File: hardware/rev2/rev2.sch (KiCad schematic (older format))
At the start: 39 parts, among them J1 Conn_01x09_Female, J2 RFM9X_header, J3 Conn_02x03_Odd_Even, U2 MPL3115A2, U3 Teensy3.6, U5 ADXL345BCCZ, U7 TPS2113ADRBR

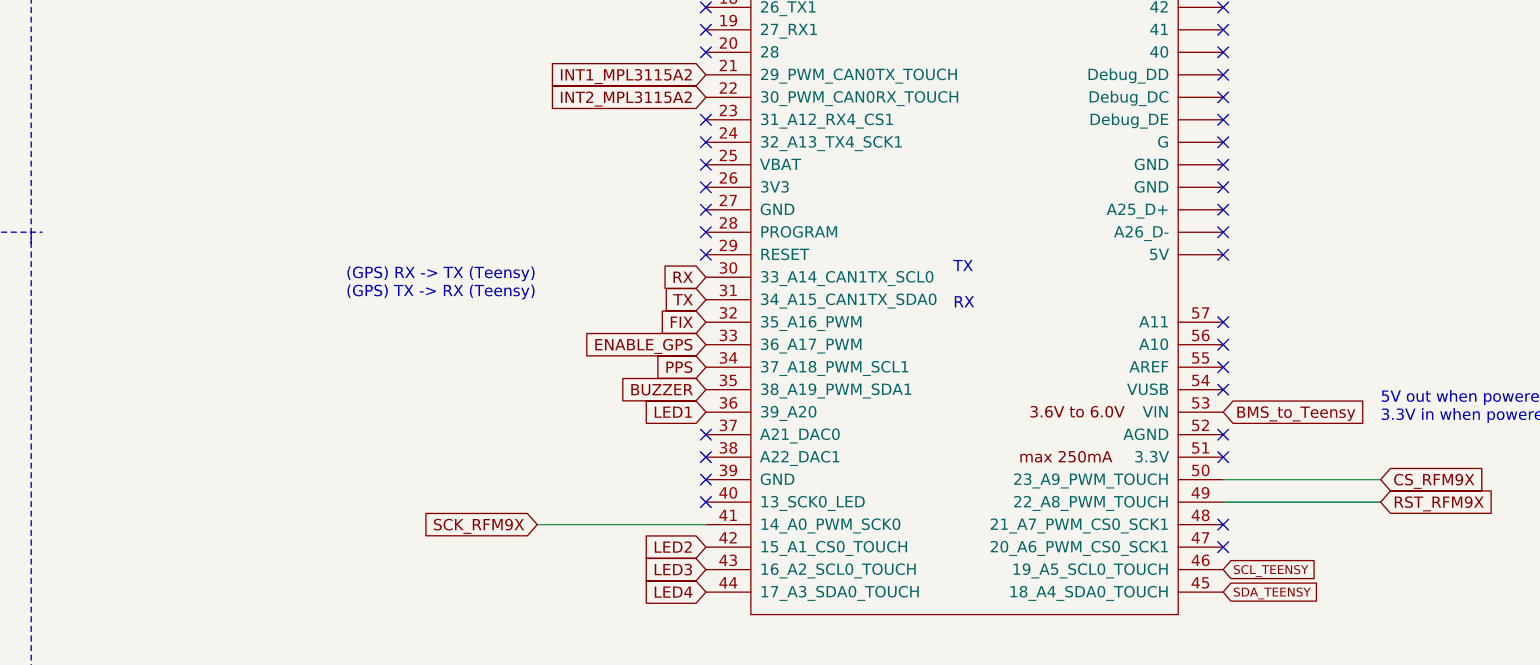
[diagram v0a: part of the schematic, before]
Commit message: connect LEDs to Teensy, add ground connections
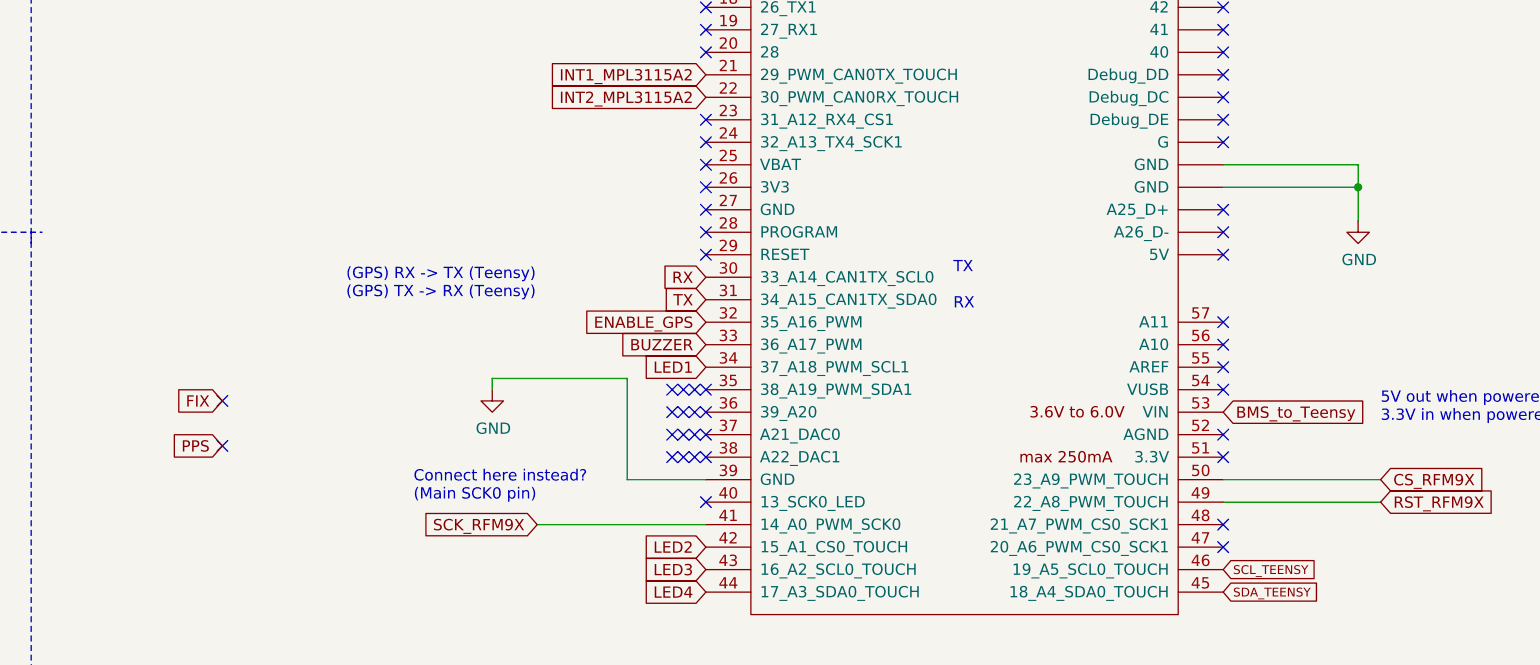
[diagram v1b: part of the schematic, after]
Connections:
- net BUZZER: now also U3.33 (36_A17_PWM); no longer U3.35 (38_A19_PWM_SDA1)
- net ENABLE_GPS: now also U3.32 (35_A16_PWM); no longer U3.33 (36_A17_PWM)
- net FIX: no longer U3.32 (35_A16_PWM)
- net GND: now also U3.39 (GND), U3.~ (GND)
- net LED1: now also U3.34 (37_A18_PWM_SCL1); no longer U3.36 (39_A20)
- net PPS: no longer U3.34 (37_A18_PWM_SCL1)
- no-connect marks 70 -> 83
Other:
- note added: "Connect here instead?\n(Main SCK0 pin)"
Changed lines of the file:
@@
 NoConn ~ 27650 10100
 NoConn ~ 27650 10200
-NoConn ~ 27650 10300
 NoConn ~ 27650 10400
 NoConn ~ 29950 10600
@@
 NoConn ~ 29950 9200
 NoConn ~ 29950 9100
-NoConn ~ 29950 9000
-NoConn ~ 29950 8900
 NoConn ~ 29950 8800
 NoConn ~ 29950 8700
@@
 TX
 Text GLabel 27650 9600 0    50   Input ~ 0
-FIX
-Text GLabel 27650 9700 0    50   Input ~ 0
 ENABLE_GPS
 NoConn ~ 29950 7100
@@
 NoConn ~ 29950 7400
 NoConn ~ 29950 7500
-Text GLabel 27650 9800 0    50   Input ~ 0
-PPS
 $Comp
 L Connector:Conn_01x09_Female J1
@@
 Wire Wire Line
 	25650 18900 25650 19050
-Text GLabel 27650 9900 0    50   Input ~ 0
+Text GLabel 27650 9700 0    50   Input ~ 0
 BUZZER
 NoConn ~ 27650 7300
@@
 Wire Wire Line
 	29550 15300 29550 15700
-Text GLabel 27650 10000 0    50   Input ~ 0
+Text GLabel 27650 9800 0    50   Input ~ 0
 LED1
 Text GLabel 27650 10600 0    50   Input ~ 0
@@
 Text GLabel 27650 10800 0    50   Input ~ 0
 LED4
+Text Notes 26350 10400 0    50   ~ 0
+Connect here instead?\n(Main SCK0 pin)
+Text GLabel 25500 10150 0    50   Input ~ 0
+PPS
+Text GLabel 25500 9950 0    50   Input ~ 0
+FIX
+NoConn ~ 27650 9900
+NoConn ~ 27650 10000
+NoConn ~ 25500 9950
+NoConn ~ 25500 10150
+NoConn ~ 27600 9900
+NoConn ~ 27550 9900
+NoConn ~ 27500 9900
+NoConn ~ 27600 10000
+NoConn ~ 27550 10000
+NoConn ~ 27500 10000
+NoConn ~ 27600 10100
+NoConn ~ 27550 10100
+NoConn ~ 27500 10100
+NoConn ~ 27600 10200
+NoConn ~ 27550 10200
+NoConn ~ 27500 10200
+$Comp
+L power:GND #PWR?
+U 1 1 606E440E
+P 26700 9900
+F 0 "#PWR?" H 26700 9650 50  0001 C CNN
+F 1 "GND" H 26705 9727 50  0000 C CNN
+F 2 "" H 26700 9900 50  0001 C CNN
+F 3 "" H 26700 9900 50  0001 C CNN
+	1    26700 9900
+	1    0    0    -1
+$EndComp
+Wire Wire Line
+	27650 10300 27300 10300
+Wire Wire Line
+	27300 10300 27300 9850
+Wire Wire Line
+	27300 9850 26700 9850
+Wire Wire Line
+	26700 9850 26700 9900
+Wire Wire Line
+	29950 8900 30550 8900
+Wire Wire Line
+	29950 9000 30550 9000
+$Comp
+L power:GND #PWR?
+U 1 1 606F48A4
+P 30550 9150
+F 0 "#PWR?" H 30550 8900 50  0001 C CNN
+F 1 "GND" H 30555 8977 50  0000 C CNN
+F 2 "" H 30550 9150 50  0001 C CNN
+F 3 "" H 30550 9150 50  0001 C CNN
+	1    30550 9150
+	1    0    0    -1
+$EndComp
+Wire Wire Line
+	30550 8900 30550 9000
+Wire Wire Line
+	30550 9000 30550 9150
+Connection ~ 30550 9000
 $EndSCHEMATC

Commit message: add KingpinLED footprint
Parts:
- D1: renamed from D?; symbol Device:D_Zener -> Device:D_Zener_x2_KCom_AAK
- D2, D3, D4, D5, D6, D7: renamed from D?; footprint (none) -> KingbrightLED:AA3528LSECKT-J4
- R10, R11, R12, R4, R8, R9: renamed from R?; footprint (none) -> footprints:R_0805_OEM
- gave numbers to parts that had none: 2
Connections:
- net BMS_to_Teensy: now also D1.3 (K); no longer D1.1 (K)
- net GND: now also D1.1 (A); no longer D1.2 (A)
- no-connect marks 83 -> 84
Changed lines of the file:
@@
 NoConn ~ 27650 6600
 $Comp
-L Device:LED D?
+L Device:LED D3
 U 1 1 6067C279
 P 24750 19750
-F 0 "D?" V 24789 19632 50  0000 R CNN
+F 0 "D3" V 24789 19632 50  0000 R CNN
 F 1 "LED" V 24698 19632 50  0000 R CNN
-F 2 "" H 24750 19750 50  0001 C CNN
+F 2 "KingbrightLED:AA3528LSECKT-J4" H 24750 19750 50  0001 C CNN
 F 3 "~" H 24750 19750 50  0001 C CNN
 	1    24750 19750
@@
 $EndComp
 $Comp
-L Device:LED D?
+L Device:LED D2
 U 1 1 60683FF2
 P 22700 19550
-F 0 "D?" V 22647 19630 50  0000 L CNN
+F 0 "D2" V 22647 19630 50  0000 L CNN
 F 1 "LED" V 22738 19630 50  0000 L CNN
-F 2 "" H 22700 19550 50  0001 C CNN
+F 2 "KingbrightLED:AA3528LSECKT-J4" H 22700 19550 50  0001 C CNN
 F 3 "~" H 22700 19550 50  0001 C CNN
 	1    22700 19550
@@
 $EndComp
 $Comp
-L Device:D_Zener D?
-U 1 1 60685331
-P 14000 19350
-F 0 "D?" V 13954 19430 50  0000 L CNN
-F 1 "D_Zener" V 14045 19430 50  0000 L CNN
-F 2 "Package_TO_SOT_SMD:SOT-23" H 14000 19350 50  0001 C CNN
-F 3 "http://www.smc-diodes.com/propdf/S23C03%20THRU%20S23C36%20N1001%20REV.A.pdf" H 14000 19350 50  0001 C CNN
-	1    14000 19350
-	0    1    1    0
-$EndComp
-$Comp
-L Device:R R?
+L Device:R R3
 U 1 1 60685DD7
 P 13400 18950
-F 0 "R?" V 13193 18950 50  0000 C CNN
+F 0 "R3" V 13193 18950 50  0000 C CNN
 F 1 "R_20" V 13284 18950 50  0000 C CNN
 F 2 "footprints:R_0805_OEM" V 13330 18950 50  0001 C CNN
@@
 $EndComp
 Wire Wire Line
-	13550 18950 14000 18950
-Wire Wire Line
-	14000 18950 14000 19200
-Wire Wire Line
 	13250 18950 12750 18950
 Wire Wire Line
 	12750 18950 12750 18550
-Connection ~ 14000 18950
-Wire Wire Line
-	14000 19500 14000 19850
-$Comp
-L power:GND #PWR?
+$Comp
+L power:GND #PWR0111
 U 1 1 606929F5
-P 14000 19850
-F 0 "#PWR?" H 14000 19600 50  0001 C CNN
-F 1 "GND" H 14005 19677 50  0000 C CNN
-F 2 "" H 14000 19850 50  0001 C CNN
-F 3 "" H 14000 19850 50  0001 C CNN
-	1    14000 19850
-	1    0    0    -1
-$EndComp
-Wire Wire Line
-	14000 18950 14650 18950
+P 14000 20550
+F 0 "#PWR0111" H 14000 20300 50  0001 C CNN
+F 1 "GND" H 14005 20377 50  0000 C CNN
+F 2 "" H 14000 20550 50  0001 C CNN
+F 3 "" H 14000 20550 50  0001 C CNN
+	1    14000 20550
+	1    0    0    -1
+$EndComp
 Text GLabel 5800 21150 3    50   Input ~ 0
 BMS_TO_ZENER
@@
 Needs to be connected to "pins" 1 and 3 on the footprint
 $Comp
-L preferred_parts:C_10uF C?
+L preferred_parts:C_10uF C1
 U 1 1 606C063B
 P 20100 11950
-F 0 "C?" H 20215 11996 50  0000 L CNN
+F 0 "C1" H 20215 11996 50  0000 L CNN
 F 1 "C_10uF" H 20215 11905 50  0000 L CNN
 F 2 "footprints:C_0805_OEM" H 20138 11800 50  0001 C CNN
@@
 	20600 12100 20600 12150
 $Comp
-L Device:R R?
+L Device:R R8
 U 1 1 606C8B99
 P 24750 19300
-F 0 "R?" H 24820 19346 50  0000 L CNN
+F 0 "R8" H 24820 19346 50  0000 L CNN
 F 1 "R_750" H 24820 19255 50  0000 L CNN
-F 2 "" V 24680 19300 50  0001 C CNN
+F 2 "footprints:R_0805_OEM" V 24680 19300 50  0001 C CNN
 F 3 "~" H 24750 19300 50  0001 C CNN
 	1    24750 19300
@@
 	25650 20000 25650 20250
 $Comp
-L Device:R R?
+L Device:R R4
 U 1 1 606DCD36
 P 22700 19050
-F 0 "R?" H 22630 19004 50  0000 R CNN
+F 0 "R4" H 22630 19004 50  0000 R CNN
 F 1 "R_750" H 22630 19095 50  0000 R CNN
-F 2 "" V 22630 19050 50  0001 C CNN
+F 2 "footprints:R_0805_OEM" V 22630 19050 50  0001 C CNN
 F 3 "~" H 22700 19050 50  0001 C CNN
 	1    22700 19050
@@
 	22700 19700 22700 19950
 $Comp
-L power:GND #PWR?
+L power:GND #PWR0112
 U 1 1 6070838D
 P 22700 19950
-F 0 "#PWR?" H 22700 19700 50  0001 C CNN
+F 0 "#PWR0112" H 22700 19700 50  0001 C CNN
 F 1 "GND" H 22705 19777 50  0000 C CNN
 F 2 "" H 22700 19950 50  0001 C CNN
@@
 	22700 18650 22700 18450
 $Comp
-L Device:LED D?
+L Device:LED D4
 U 1 1 6071A190
 P 27300 16550
-F 0 "D?" V 27247 16630 50  0000 L CNN
+F 0 "D4" V 27247 16630 50  0000 L CNN
 F 1 "LED" V 27338 16630 50  0000 L CNN
-F 2 "" H 27300 16550 50  0001 C CNN
+F 2 "KingbrightLED:AA3528LSECKT-J4" H 27300 16550 50  0001 C CNN
 F 3 "~" H 27300 16550 50  0001 C CNN
 	1    27300 16550
@@
 $EndComp
 $Comp
-L Device:LED D?
+L Device:LED D5
 U 1 1 6071B08F
 P 28050 16550
-F 0 "D?" V 27997 16630 50  0000 L CNN
+F 0 "D5" V 27997 16630 50  0000 L CNN
 F 1 "LED" V 28088 16630 50  0000 L CNN
-F 2 "" H 28050 16550 50  0001 C CNN
+F 2 "KingbrightLED:AA3528LSECKT-J4" H 28050 16550 50  0001 C CNN
 F 3 "~" H 28050 16550 50  0001 C CNN
 	1    28050 16550
@@
 $EndComp
 $Comp
-L Device:LED D?
+L Device:LED D6
 U 1 1 6071B76B
 P 28800 16550
-F 0 "D?" V 28747 16630 50  0000 L CNN
+F 0 "D6" V 28747 16630 50  0000 L CNN
 F 1 "LED" V 28838 16630 50  0000 L CNN
-F 2 "" H 28800 16550 50  0001 C CNN
+F 2 "KingbrightLED:AA3528LSECKT-J4" H 28800 16550 50  0001 C CNN
 F 3 "~" H 28800 16550 50  0001 C CNN
 	1    28800 16550
@@
 $EndComp
 $Comp
-L Device:LED D?
+L Device:LED D7
 U 1 1 6071C533
 P 29550 16550
-F 0 "D?" V 29497 16630 50  0000 L CNN
+F 0 "D7" V 29497 16630 50  0000 L CNN
 F 1 "LED" V 29588 16630 50  0000 L CNN
-F 2 "" H 29550 16550 50  0001 C CNN
+F 2 "KingbrightLED:AA3528LSECKT-J4" H 29550 16550 50  0001 C CNN
 F 3 "~" H 29550 16550 50  0001 C CNN
 	1    29550 16550
@@
 $EndComp
 $Comp
-L Device:R R?
+L Device:R R9
 U 1 1 6071C81F
 P 27300 15850
-F 0 "R?" H 27230 15804 50  0000 R CNN
+F 0 "R9" H 27230 15804 50  0000 R CNN
 F 1 "R_750" H 27230 15895 50  0000 R CNN
-F 2 "" V 27230 15850 50  0001 C CNN
+F 2 "footprints:R_0805_OEM" V 27230 15850 50  0001 C CNN
 F 3 "~" H 27300 15850 50  0001 C CNN
 	1    27300 15850
@@
 $EndComp
 $Comp
-L Device:R R?
+L Device:R R10
 U 1 1 6071D566
 P 28050 15850
-F 0 "R?" H 27980 15804 50  0000 R CNN
+F 0 "R10" H 27980 15804 50  0000 R CNN
 F 1 "R_750" H 27980 15895 50  0000 R CNN
-F 2 "" V 27980 15850 50  0001 C CNN
+F 2 "footprints:R_0805_OEM" V 27980 15850 50  0001 C CNN
 F 3 "~" H 28050 15850 50  0001 C CNN
 	1    28050 15850
@@
 $EndComp
 $Comp
-L Device:R R?
+L Device:R R11
 U 1 1 6071D762
 P 28800 15850
-F 0 "R?" H 28730 15804 50  0000 R CNN
+F 0 "R11" H 28730 15804 50  0000 R CNN
 F 1 "R_750" H 28730 15895 50  0000 R CNN
-F 2 "" V 28730 15850 50  0001 C CNN
+F 2 "footprints:R_0805_OEM" V 28730 15850 50  0001 C CNN
 F 3 "~" H 28800 15850 50  0001 C CNN
 	1    28800 15850
@@
 $EndComp
 $Comp
-L Device:R R?
+L Device:R R12
 U 1 1 6071D979
 P 29550 15850
-F 0 "R?" H 29480 15804 50  0000 R CNN
+F 0 "R12" H 29480 15804 50  0000 R CNN
 F 1 "R_750" H 29480 15895 50  0000 R CNN
-F 2 "" V 29480 15850 50  0001 C CNN
+F 2 "footprints:R_0805_OEM" V 29480 15850 50  0001 C CNN
 F 3 "~" H 29550 15850 50  0001 C CNN
 	1    29550 15850
@@
 	29550 16000 29550 16400
 $Comp
-L power:GND #PWR?
+L power:GND #PWR0113
 U 1 1 6072D642
 P 29550 17250
-F 0 "#PWR?" H 29550 17000 50  0001 C CNN
+F 0 "#PWR0113" H 29550 17000 50  0001 C CNN
 F 1 "GND" H 29555 17077 50  0000 C CNN
 F 2 "" H 29550 17250 50  0001 C CNN
@@
 NoConn ~ 27500 10200
 $Comp
-L power:GND #PWR?
+L power:GND #PWR0114
 U 1 1 606E440E
 P 26700 9900
-F 0 "#PWR?" H 26700 9650 50  0001 C CNN
+F 0 "#PWR0114" H 26700 9650 50  0001 C CNN
 F 1 "GND" H 26705 9727 50  0000 C CNN
 F 2 "" H 26700 9900 50  0001 C CNN
@@
 	29950 9000 30550 9000
 $Comp
-L power:GND #PWR?
+L power:GND #PWR0116
 U 1 1 606F48A4
 P 30550 9150
-F 0 "#PWR?" H 30550 8900 50  0001 C CNN
+F 0 "#PWR0116" H 30550 8900 50  0001 C CNN
 F 1 "GND" H 30555 8977 50  0000 C CNN
 F 2 "" H 30550 9150 50  0001 C CNN
@@
 	30550 9000 30550 9150
 Connection ~ 30550 9000
+Wire Wire Line
+	14000 20000 14000 20550
+Wire Wire Line
+	14200 19700 14600 19700
+Wire Wire Line
+	14600 19700 14600 18950
+Connection ~ 14600 18950
+Wire Wire Line
+	14600 18950 14650 18950
+Wire Wire Line
+	13550 18950 14600 18950
+$Comp
+L Device:D_Zener_x2_KCom_AAK D1
+U 1 1 60685331
+P 14000 19700
+F 0 "D1" V 13954 19780 50  0000 L CNN
+F 1 "D_Zener" V 14045 19780 50  0000 L CNN
+F 2 "Package_TO_SOT_SMD:SOT-23" H 14000 19700 50  0001 C CNN
+F 3 "http://www.smc-diodes.com/propdf/S23C03%20THRU%20S23C36%20N1001%20REV.A.pdf" H 14000 19700 50  0001 C CNN
+	1    14000 19700
+	0    -1   -1   0
+$EndComp
+NoConn ~ 14000 19400
 $EndSCHEMATC

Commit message: remove test points from schematic
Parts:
- removed CAP2, GND1, GND2, VDD1, VDD2: TestPoint, footprints:Test-Point-Pin_Drill2.79mm, symbol Connector:TestPoint
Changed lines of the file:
@@
 	1    0    0    -1
 $EndComp
-Wire Wire Line
-	11450 12750 11200 12750
 Connection ~ 11100 13050
 Wire Wire Line
@@
 Wire Wire Line
 	10200 13050 10200 13200
-$Comp
-L power:GNDPWR #PWR0101
-U 1 1 5FA0E6D7
-P 14150 13100
-F 0 "#PWR0101" H 14150 12900 50  0001 C CNN
-F 1 "GNDPWR" H 14154 12946 50  0000 C CNN
-F 2 "" H 14150 13050 50  0001 C CNN
-F 3 "" H 14150 13050 50  0001 C CNN
-	1    14150 13100
-	1    0    0    -1
-$EndComp
 Text GLabel 12350 12650 2    50   Input ~ 0
 SCL_TEENSY
@@
 Wire Wire Line
 	10200 13050 10700 13050
-$Comp
-L power:GND #PWR0104
-U 1 1 5FA275B3
-P 13750 13100
-F 0 "#PWR0104" H 13750 12850 50  0001 C CNN
-F 1 "GND" H 13755 12927 50  0000 C CNN
-F 2 "" H 13750 13100 50  0001 C CNN
-F 3 "" H 13750 13100 50  0001 C CNN
-	1    13750 13100
-	1    0    0    -1
-$EndComp
-Wire Wire Line
-	13750 13000 13750 13100
-Wire Wire Line
-	13750 12750 13750 12850
-$Comp
-L Connector:TestPoint CAP2
-U 1 1 5FEA9553
-P 11200 11850
-F 0 "CAP2" H 11258 11968 50  0000 L CNN
-F 1 "TestPoint" H 11258 11877 50  0000 L CNN
-F 2 "footprints:Test-Point-Pin_Drill2.79mm" H 11400 11850 50  0001 C CNN
-F 3 "~" H 11400 11850 50  0001 C CNN
-	1    11200 11850
-	1    0    0    -1
-$EndComp
-Wire Wire Line
-	11200 11850 11200 12750
-Connection ~ 11200 12750
-Wire Wire Line
-	11200 12750 11100 12750
-$Comp
-L Connector:TestPoint VDD2
-U 1 1 60279C64
-P 14550 12850
-F 0 "VDD2" H 14608 12968 50  0000 L CNN
-F 1 "TestPoint" H 14608 12877 50  0000 L CNN
-F 2 "footprints:Test-Point-Pin_Drill2.79mm" H 14750 12850 50  0001 C CNN
-F 3 "~" H 14750 12850 50  0001 C CNN
-	1    14550 12850
-	1    0    0    -1
-$EndComp
-$Comp
-L Connector:TestPoint GND2
-U 1 1 60279C65
-P 14550 13000
-F 0 "GND2" H 14608 13118 50  0000 L CNN
-F 1 "TestPoint" H 14608 13027 50  0000 L CNN
-F 2 "footprints:Test-Point-Pin_Drill2.79mm" H 14750 13000 50  0001 C CNN
-F 3 "~" H 14750 13000 50  0001 C CNN
-	1    14550 13000
-	-1   0    0    1
-$EndComp
-Wire Wire Line
-	13750 13000 14150 13000
-Wire Wire Line
-	14150 13100 14150 13000
-Connection ~ 14150 13000
-Wire Wire Line
-	14150 13000 14550 13000
 Text Notes 9900 11050 0    197  ~ 0
 MPL3115A2 (Altimeter)
@@
 	1    0    0    -1
 $EndComp
-$Comp
-L Connector:TestPoint VDD1
-U 1 1 5FF680D8
-P 23100 18750
-F 0 "VDD1" H 23042 18776 50  0000 R CNN
-F 1 "TestPoint" H 23042 18867 50  0000 R CNN
-F 2 "footprints:Test-Point-Pin_Drill2.79mm" H 23300 18750 50  0001 C CNN
-F 3 "~" H 23300 18750 50  0001 C CNN
-	1    23100 18750
-	-1   0    0    1
-$EndComp
-$Comp
-L Connector:TestPoint GND1
-U 1 1 5FF68D98
-P 20950 18750
-F 0 "GND1" H 20892 18776 50  0000 R CNN
-F 1 "TestPoint" H 20892 18867 50  0000 R CNN
-F 2 "footprints:Test-Point-Pin_Drill2.79mm" H 21150 18750 50  0001 C CNN
-F 3 "~" H 21150 18750 50  0001 C CNN
-	1    20950 18750
-	1    0    0    -1
-$EndComp
-Wire Wire Line
-	20950 18750 20950 18950
-Connection ~ 20950 18950
 Wire Notes Line width 12
 	16100 9200 16100 450
@@
 NoConn ~ 29950 6600
 NoConn ~ 29950 6500
-$Comp
-L power:+3.3V #PWR0103
-U 1 1 60279C5C
-P 13750 12750
-F 0 "#PWR0103" H 13750 12600 50  0001 C CNN
-F 1 "+3.3V" H 13765 12923 50  0000 C CNN
-F 2 "" H 13750 12750 50  0001 C CNN
-F 3 "" H 13750 12750 50  0001 C CNN
-	1    13750 12750
-	1    0    0    -1
-$EndComp
 NoConn ~ 27650 8000
 NoConn ~ 27650 8100
@@
 Wire Wire Line
 	11450 13350 11250 13350
-Wire Wire Line
-	13750 12850 14550 12850
 Text GLabel 27650 7900 0    39   Input ~ 0
 3.3V_TEENSY
@@
 	1    0    0    -1
 $EndComp
-Wire Wire Line
-	22700 18900 22700 18650
-Wire Wire Line
-	22700 18650 23100 18650
-Wire Wire Line
-	23100 18650 23100 18750
-Connection ~ 22700 18650
-Wire Wire Line
-	22700 18650 22700 18450
 $Comp
 L Device:LED D4
@@
 $EndComp
 NoConn ~ 14000 19400
+Wire Wire Line
+	11100 12750 11450 12750
+Wire Wire Line
+	22700 18450 22700 18900
 $EndSCHEMATC

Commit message: rev2 ready for checkoff
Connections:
- net +3V3: now also U3.51 (3.3V)
- net 3.3VBMS: now also J3.2 (Pin_2); no longer J3.3 (Pin_3)
- net 3.3VBMS_Backup: now also J3.4 (Pin_4); no longer J3.5 (Pin_5)
- net DROGUE_DEPLOY: now also J3.5 (Pin_5); no longer J3.4 (Pin_4)
- net MAIN_DEPLOY: now also J3.6 (Pin_6); no longer J3.2 (Pin_2)
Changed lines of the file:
@@
 NoConn ~ 29950 10600
 NoConn ~ 29950 10500
-NoConn ~ 29950 10200
 NoConn ~ 29950 10100
 NoConn ~ 29950 9900
@@
 Wire Wire Line
 	2400 21300 1500 21300
-Text GLabel 2400 21400 0    50   Input ~ 0
+Text GLabel 2900 21300 2    50   Input ~ 0
 3.3VBMS
 Text GLabel 5600 18550 1    50   Input ~ 0
@@
 Text GLabel 5500 18550 1    50   Input ~ 0
 3.3VBMS_Backup
-Text GLabel 2400 21500 0    50   Input ~ 0
+Text GLabel 2900 21400 2    50   Input ~ 0
 3.3VBMS_Backup
 $Comp
@@
 	2550 19850 2550 19700
 Connection ~ 2550 19850
-Text GLabel 2900 21300 2    50   Input ~ 0
+Text GLabel 2900 21500 2    50   Input ~ 0
 MAIN_DEPLOY
-Text GLabel 2900 21400 2    50   Input ~ 0
+Text GLabel 2400 21500 0    50   Input ~ 0
 DROGUE_DEPLOY
 $Comp
@@
 Wire Wire Line
 	22700 18450 22700 18900
+Text GLabel 29950 10200 2    39   Input ~ 0
+3.3V_TEENSY
+NoConn ~ 2400 21400
 $EndSCHEMATC
